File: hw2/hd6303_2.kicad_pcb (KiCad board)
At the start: 2 copper layers, 29 parts, among them J1 Conn_02x20_Odd_Even, J2 Conn_02x06_Odd_Even, J3 Screw_Terminal_01x02, SW1 SW_Push, U2 MAX708, U3 27C512, U4 HD6303RP, U5 HM62256BLP-7, U6 GAL16V8, Y1 4.9152M

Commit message: some tidying up
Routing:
- net /-RMEM: track 99.5 -> 100.2 mm
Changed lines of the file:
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@@
     (thickness 1.6)
     (drawings 0)
-    (tracks 969)
+    (tracks 982)
     (zones 0)
     (modules 29)
@@
   (segment (start 87.884 90.424) (end 87.884 93.98) (width 0.1524) (layer B.Cu) (net 1))
   (segment (start 87.884 93.98) (end 86.868 94.996) (width 0.1524) (layer B.Cu) (net 1))
+  (segment (start 143.73352 138.41984) (end 145.70456 138.41984) (width 0.254) (layer B.Cu) (net 2))
+  (segment (start 142.4178 137.10412) (end 143.73352 138.41984) (width 0.254) (layer B.Cu) (net 2))
+  (segment (start 145.6944 138.44016) (end 145.70964 138.4554) (width 0.254) (layer F.Cu) (net 2))
+  (segment (start 145.70964 138.42492) (end 145.6944 138.44016) (width 0.254) (layer F.Cu) (net 2))
+  (via (at 145.70964 138.42492) (size 0.6858) (drill 0.3302) (layers F.Cu B.Cu) (net 2))
+  (segment (start 145.70456 138.41984) (end 145.70964 138.42492) (width 0.254) (layer B.Cu) (net 2))
   (segment (start 164.592 139.7) (end 164.592 139.78128) (width 0.254) (layer F.Cu) (net 2))
   (segment (start 164.592 139.78128) (end 163.41852 140.95476) (width 0.254) (layer F.Cu) (net 2))
-  (segment (start 143.73352 138.41984) (end 142.4178 137.10412) (width 0.254) (layer B.Cu) (net 2))
-  (via (at 143.73352 138.41984) (size 0.6858) (drill 0.3302) (layers F.Cu B.Cu) (net 2))
-  (segment (start 143.75384 138.44016) (end 143.73352 138.41984) (width 0.254) (layer F.Cu) (net 2))
-  (segment (start 150.99792 138.44016) (end 143.75384 138.44016) (width 0.254) (layer F.Cu) (net 2))
+  (segment (start 163.41852 140.95476) (end 160.12668 140.95476) (width 0.254) (layer F.Cu) (net 2))
+  (segment (start 160.12668 140.95476) (end 159.37992 140.208) (width 0.254) (layer F.Cu) (net 2))
+  (segment (start 159.37992 140.208) (end 152.76576 140.208) (width 0.254) (layer F.Cu) (net 2))
   (segment (start 152.76576 140.208) (end 150.99792 138.44016) (width 0.254) (layer F.Cu) (net 2))
-  (segment (start 159.37992 140.208) (end 152.76576 140.208) (width 0.254) (layer F.Cu) (net 2))
-  (segment (start 160.12668 140.95476) (end 159.37992 140.208) (width 0.254) (layer F.Cu) (net 2))
-  (segment (start 163.41852 140.95476) (end 160.12668 140.95476) (width 0.254) (layer F.Cu) (net 2))
+  (segment (start 150.99792 138.44016) (end 145.70964 138.4554) (width 0.254) (layer F.Cu) (net 2))
+  (segment (start 145.70964 138.4554) (end 145.68932 138.43508) (width 0.254) (layer F.Cu) (net 2))
   (segment (start 142.4178 137.10412) (end 142.4178 136.5104) (width 0.254) (layer B.Cu) (net 2))
   (segment (start 134.62 119.38) (end 134.62 108.712) (width 0.254) (layer B.Cu) (net 2))
@@
   (segment (start 157.17012 93.69552) (end 154.65552 93.69552) (width 0.1524) (layer B.Cu) (net 10))
   (segment (start 154.65552 93.69552) (end 153.416 92.456) (width 0.1524) (layer B.Cu) (net 10) (status 800000))
+  (segment (start 144.627681 136.504721) (end 144.292279 136.504721) (width 0.1524) (layer F.Cu) (net 11))
+  (segment (start 136.50468 137.81532) (end 135.84936 137.16) (width 0.1524) (layer F.Cu) (net 11))
+  (segment (start 142.98168 137.81532) (end 136.50468 137.81532) (width 0.1524) (layer F.Cu) (net 11))
+  (segment (start 144.292279 136.504721) (end 142.98168 137.81532) (width 0.1524) (layer F.Cu) (net 11))
   (segment (start 156.14904 110.70336) (end 156.46908 110.70336) (width 0.1524) (layer F.Cu) (net 11))
-  (segment (start 135.87476 137.16) (end 136.70788 137.99312) (width 0.1524) (layer F.Cu) (net 11))
-  (segment (start 136.70788 137.99312) (end 142.5702 137.99312) (width 0.1524) (layer F.Cu) (net 11))
-  (segment (start 142.5702 137.99312) (end 144.05356 136.50976) (width 0.1524) (layer F.Cu) (net 11))
-  (segment (start 144.05356 136.50976) (end 146.52244 136.50976) (width 0.1524) (layer F.Cu) (net 11))
+  (segment (start 144.61236 136.50468) (end 144.627681 136.504721) (width 0.1524) (layer F.Cu) (net 11))
+  (segment (start 144.627681 136.504721) (end 146.52244 136.50976) (width 0.1524) (layer F.Cu) (net 11))
   (via (at 146.52244 136.50976) (size 0.6858) (drill 0.3302) (layers F.Cu B.Cu) (net 11))
   (segment (start 146.52244 136.50976) (end 146.44624 136.43356) (width 0.1524) (layer B.Cu) (net 11))
@@
   (segment (start 146.44624 110.88624) (end 146.6088 110.72368) (width 0.1524) (layer F.Cu) (net 11))
   (segment (start 146.6088 110.72368) (end 156.14904 110.70336) (width 0.1524) (layer F.Cu) (net 11))
-  (segment (start 134.62 137.16) (end 135.87476 137.16) (width 0.1524) (layer F.Cu) (net 11))
+  (segment (start 134.62 137.16) (end 135.84936 137.16) (width 0.1524) (layer F.Cu) (net 11))
+  (segment (start 135.84936 137.16) (end 135.87476 137.16) (width 0.1524) (layer F.Cu) (net 11))
   (segment (start 159.9438 104.1654) (end 162.0266 104.1654) (width 0.1524) (layer F.Cu) (net 11))
   (segment (start 158.60268 105.50652) (end 159.9438 104.1654) (width 0.1524) (layer F.Cu) (net 11))
@@
   (via (at 91.059 110.871) (size 0.6858) (drill 0.3302) (layers F.Cu B.Cu) (net 26))
   (segment (start 91.186 110.744) (end 91.059 110.871) (width 0.1524) (layer F.Cu) (net 26))
+  (segment (start 144.30756 134.614961) (end 144.277039 134.614961) (width 0.1524) (layer F.Cu) (net 27))
+  (segment (start 135.91032 135.89508) (end 122.9868 135.89) (width 0.1524) (layer F.Cu) (net 27))
+  (segment (start 122.9868 135.89) (end 121.7168 134.62) (width 0.1524) (layer F.Cu) (net 27))
+  (segment (start 136.50468 135.30072) (end 135.91032 135.89508) (width 0.1524) (layer F.Cu) (net 27))
+  (segment (start 143.59128 135.30072) (end 136.50468 135.30072) (width 0.1524) (layer F.Cu) (net 27))
+  (segment (start 144.277039 134.614961) (end 143.59128 135.30072) (width 0.1524) (layer F.Cu) (net 27))
+  (segment (start 149.86 134.62) (end 144.30756 134.614961) (width 0.1524) (layer F.Cu) (net 27) (status 400000))
+  (segment (start 144.30756 134.614961) (end 144.26184 134.61492) (width 0.1524) (layer F.Cu) (net 27))
+  (segment (start 140.24864 135.0772) (end 140.23848 135.08736) (width 0.1524) (layer F.Cu) (net 27))
   (segment (start 149.86 134.62) (end 155.08224 134.62) (width 0.1524) (layer F.Cu) (net 27) (status 400000))
   (segment (start 155.31084 124.46) (end 162.052 124.46) (width 0.1524) (layer F.Cu) (net 27) (status 800000))
@@
   (segment (start 118.4148 135.7122) (end 116.2304 135.7122) (width 0.1524) (layer F.Cu) (net 27))
   (segment (start 149.86 134.62) (end 149.1996 134.62) (width 0.1524) (layer F.Cu) (net 27))
-  (segment (start 149.1996 134.62) (end 148.5392 135.2804) (width 0.1524) (layer F.Cu) (net 27))
-  (segment (start 148.5392 135.2804) (end 141.3764 135.2804) (width 0.1524) (layer F.Cu) (net 27))
-  (segment (start 141.3764 135.2804) (end 140.7668 135.89) (width 0.1524) (layer F.Cu) (net 27))
-  (segment (start 140.7668 135.89) (end 122.9868 135.89) (width 0.1524) (layer F.Cu) (net 27))
-  (segment (start 122.9868 135.89) (end 121.7168 134.62) (width 0.1524) (layer F.Cu) (net 27))
   (segment (start 121.7168 134.62) (end 120.65 134.62) (width 0.1524) (layer F.Cu) (net 27))
   (segment (start 134.62 149.86) (end 135.82904 149.86) (width 0.1524) (layer F.Cu) (net 28))
@@
   (segment (start 149.86 139.7) (end 149.7076 139.7) (width 0.1524) (layer F.Cu) (net 49))
   (segment (start 111.0488 104.6988) (end 110.49 104.14) (width 0.1524) (layer F.Cu) (net 49))
-  (segment (start 149.86 137.16) (end 143.9926 137.16) (width 0.1524) (layer F.Cu) (net 50))
-  (segment (start 122.9614 138.4046) (end 121.7168 137.16) (width 0.1524) (layer F.Cu) (net 50))
+  (segment (start 144.56664 137.17524) (end 144.5514 137.17524) (width 0.1524) (layer F.Cu) (net 50))
+  (segment (start 142.6972 138.4554) (end 135.763 138.4554) (width 0.1524) (layer F.Cu) (net 50))
   (segment (start 135.763 138.4554) (end 122.9614 138.4046) (width 0.1524) (layer F.Cu) (net 50))
-  (segment (start 142.6972 138.4554) (end 135.763 138.4554) (width 0.1524) (layer F.Cu) (net 50))
-  (segment (start 143.9926 137.16) (end 142.6972 138.4554) (width 0.1524) (layer F.Cu) (net 50))
+  (segment (start 121.7168 137.16) (end 122.9614 138.4046) (width 0.1524) (layer F.Cu) (net 50))
+  (segment (start 144.56664 137.17524) (end 149.86 137.16) (width 0.1524) (layer F.Cu) (net 50) (status 800000))
+  (segment (start 143.27124 138.4554) (end 142.6972 138.4554) (width 0.1524) (layer F.Cu) (net 50))
+  (segment (start 144.5514 137.17524) (end 143.27124 138.4554) (width 0.1524) (layer F.Cu) (net 50))
   (segment (start 110.49 111.76) (end 110.49 138.7602) (width 0.1524) (layer B.Cu) (net 50))
   (via (at 110.49 138.7602) (size 0.6858) (drill 0.3302) (layers F.Cu B.Cu) (net 50))

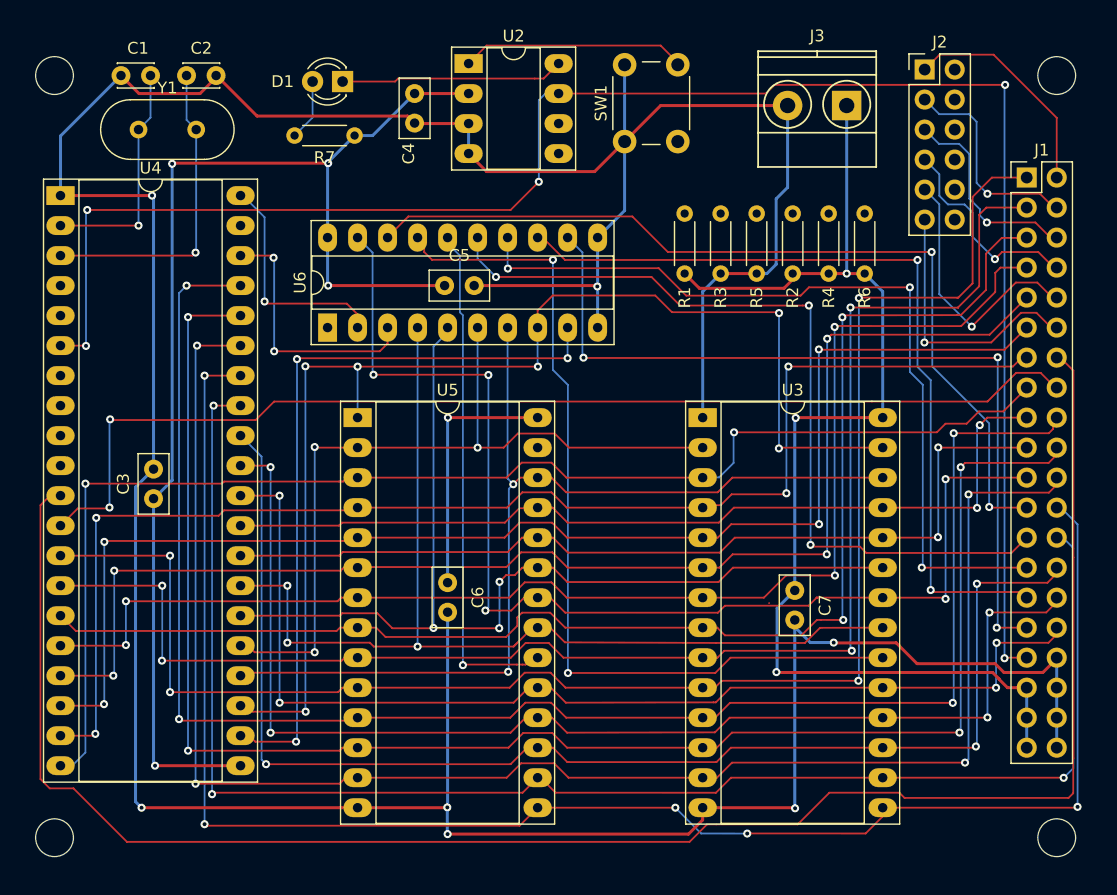
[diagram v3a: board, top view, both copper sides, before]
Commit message: all traces routed!
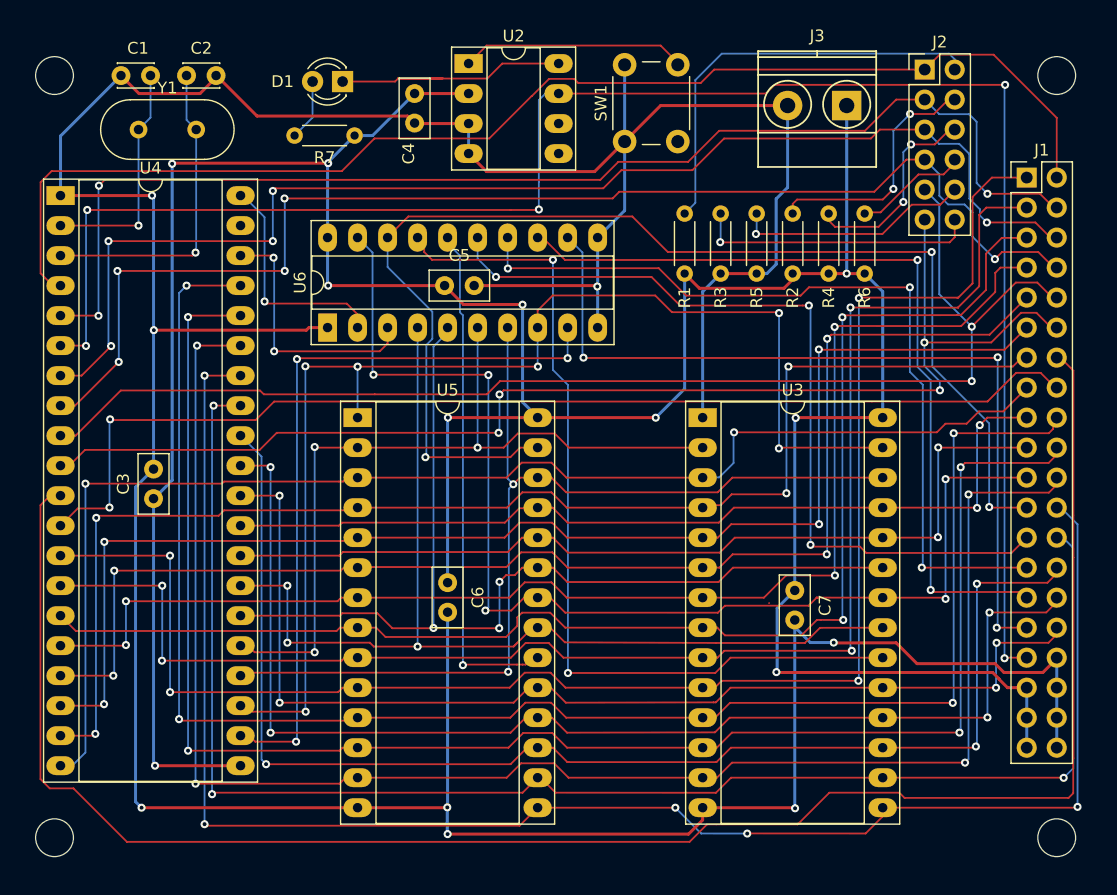
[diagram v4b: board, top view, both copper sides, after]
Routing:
- net /P20: track 17.7 -> 107.8 mm, vias 1 -> 5
- net /-STBY: track 17.5 -> 107.3 mm, vias 1 -> 5
- net /-NMI: track 19.0 -> 107.9 mm
- net /-IRQ1: track 18.0 -> 105.2 mm, vias 1 -> 3
- net /P21: track 22.5 -> 106.4 mm, vias 1 -> 2
- net /P22: track 23.2 -> 106.7 mm, vias 1 -> 4
- net VCC: track 228.9 -> 269.4 mm, vias 8 -> 10
- net Net-(J2-Pad2): track 0.00 -> 35.6 mm
- net /-WMEM: track 74.9 -> 105.1 mm, vias 2 -> 3
- net Net-(J2-Pad12): track 0.00 -> 24.0 mm, vias 0 -> 1
- net Net-(J2-Pad4): track 0.00 -> 21.1 mm, vias 0 -> 2
- net Net-(J2-Pad10): track 0.00 -> 20.2 mm, vias 0 -> 1
- net Net-(J2-Pad6): track 0.00 -> 17.4 mm, vias 0 -> 2
- net GND: track 328.2 -> 343.0 mm, vias 7 -> 8
- net Net-(J2-Pad8): track 0.00 -> 9.70 mm
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
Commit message: board outline, silkscreen tweaks
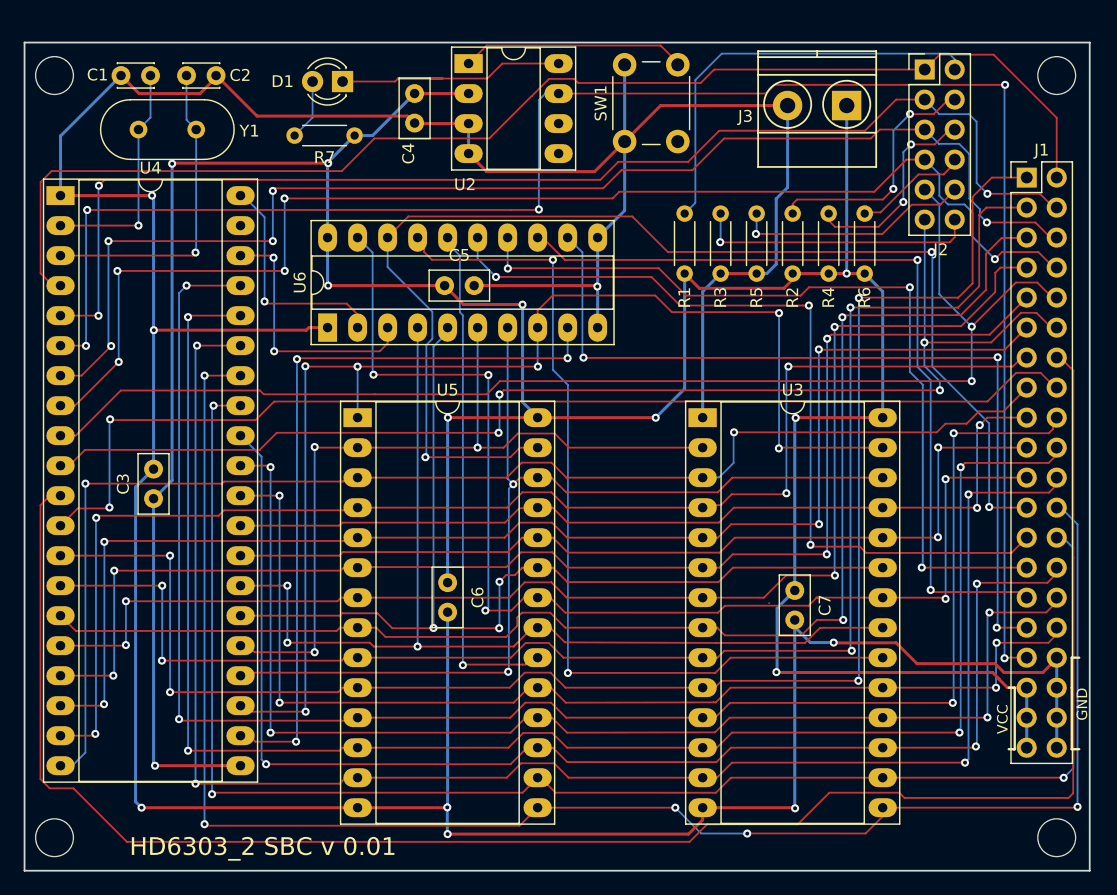
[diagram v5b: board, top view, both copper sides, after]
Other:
- board outline added: 90.2 x 70.1 mm
- board text added: "GND"
- board text added: "HD6303_2 SBC v 0.01"
- board text added: "VCC"
